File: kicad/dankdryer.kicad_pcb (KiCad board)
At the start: 2 copper layers, 100 x 75 mm, 42 parts, among them J1 Barreljack, J2 upper fan, J3 lower fan, J4 heater, J6 Screw_Terminal_01x05, J7 5kg load cell, J8 motor, J9 Conn_01x04, Q2 SSM3K127TU, Q3 T1210-800G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

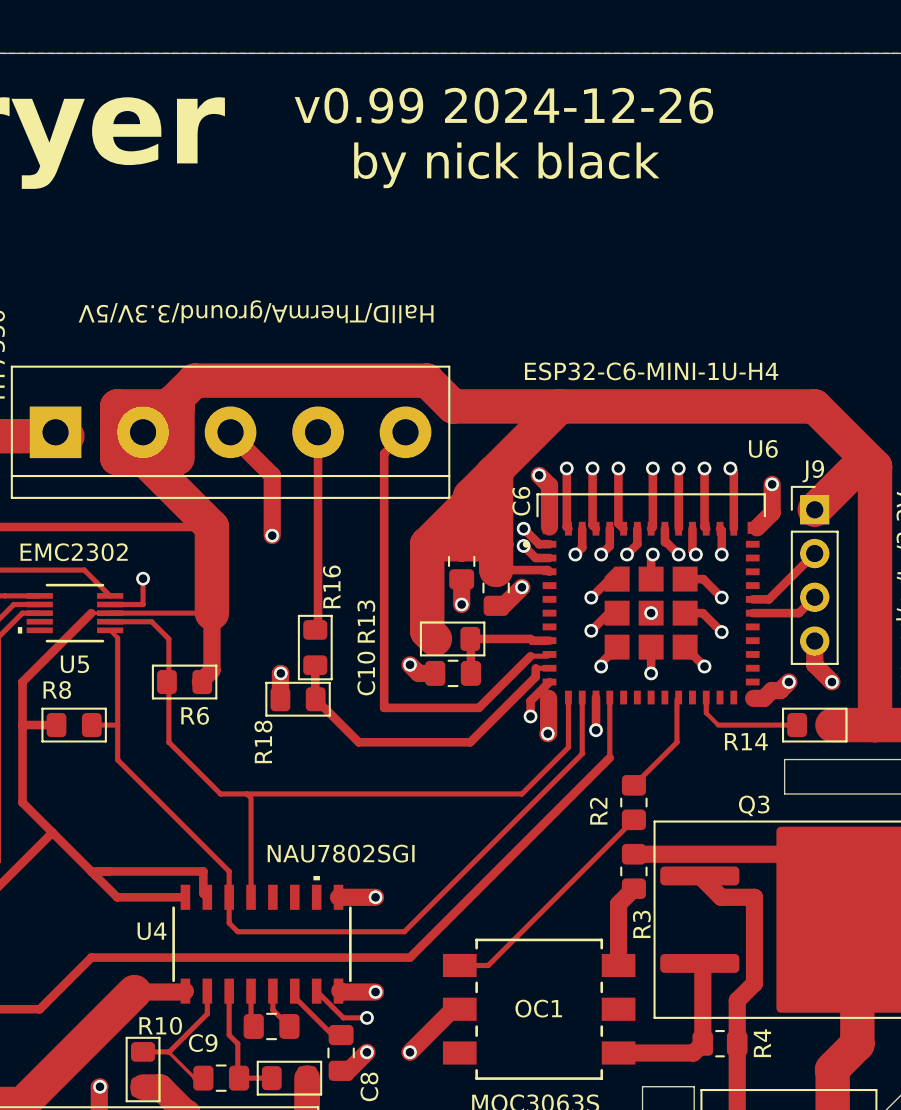
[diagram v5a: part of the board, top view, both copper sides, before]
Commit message: get off the strapping pins. hardware version 1.0
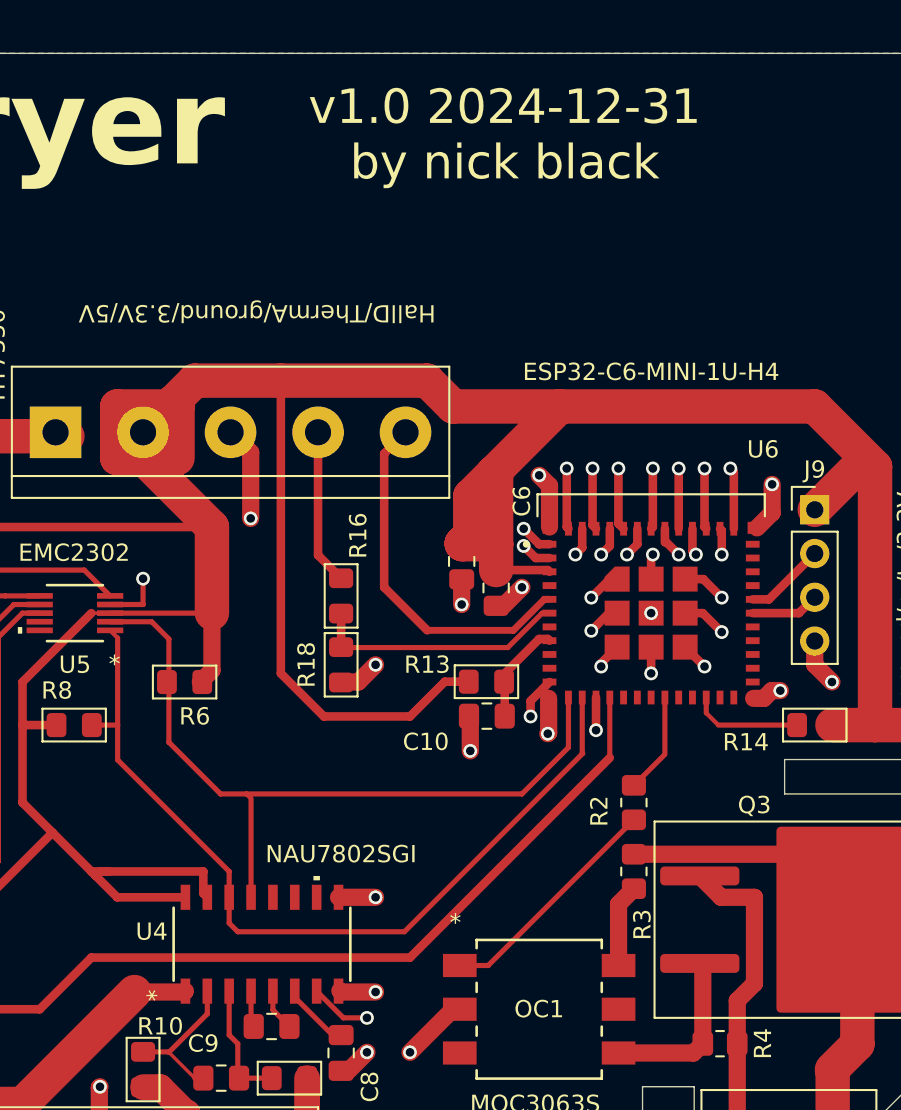
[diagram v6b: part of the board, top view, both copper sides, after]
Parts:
- moved R16 3.35 mm to (105.5, 81.5)
- moved R18 3.20 mm to (105.5, 85.5), turned to 90 degrees
- moved C10 3.16 mm to (114.0, 88.5)
- moved R13 3.16 mm to (113.9, 86.5)
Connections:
- U6 pad 10: /Therm -> unconnected-(U6-IO5-Pad10)
- U6 pad 19: unconnected-(U6-IO14-Pad19) -> /SSRControl
- U6 pad 20: /SSRControl -> unconnected-(U6-IO15-Pad20)
- U6 pad 5: unconnected-(U6-IO2-Pad5) -> /Hall
- U6 pad 6: unconnected-(U6-IO3-Pad6) -> /Therm
- U6 pad 9: /Hall -> unconnected-(U6-IO4-Pad9)
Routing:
- net +3.3V: track 349.1 -> 370.3 mm
- net /Hall: track 27.3 -> 20.9 mm
- net /Therm: track 18.6 -> 14.9 mm
- net /Hot chamber microboard/ThermAnalog: track 11.3 -> 9.03 mm
- net Net-(U6-EN): track 6.60 -> 5.49 mm
- net GND: track 139.5 -> 138.6 mm
- added copper zone on B.Cu, net unconnected-(U2-Therm-Pad9)_2
- removed copper zone on B.Cu, net unconnected-(U2-Therm-Pad9)_3
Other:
- board text added: "v1.0 2024-12-31 by nick black"
- board text removed: "v0.99 2024-12-26 by nick black"

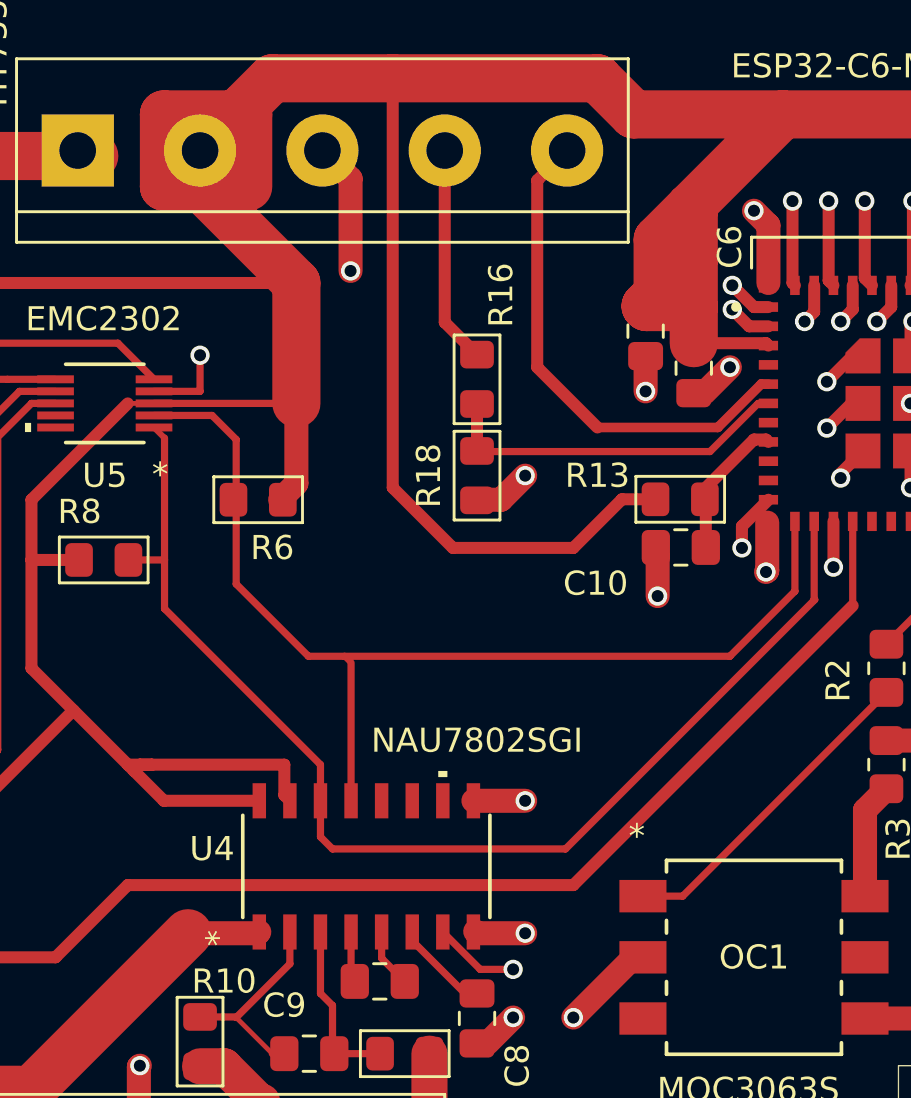
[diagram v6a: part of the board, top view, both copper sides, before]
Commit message: webpage: update copyrights
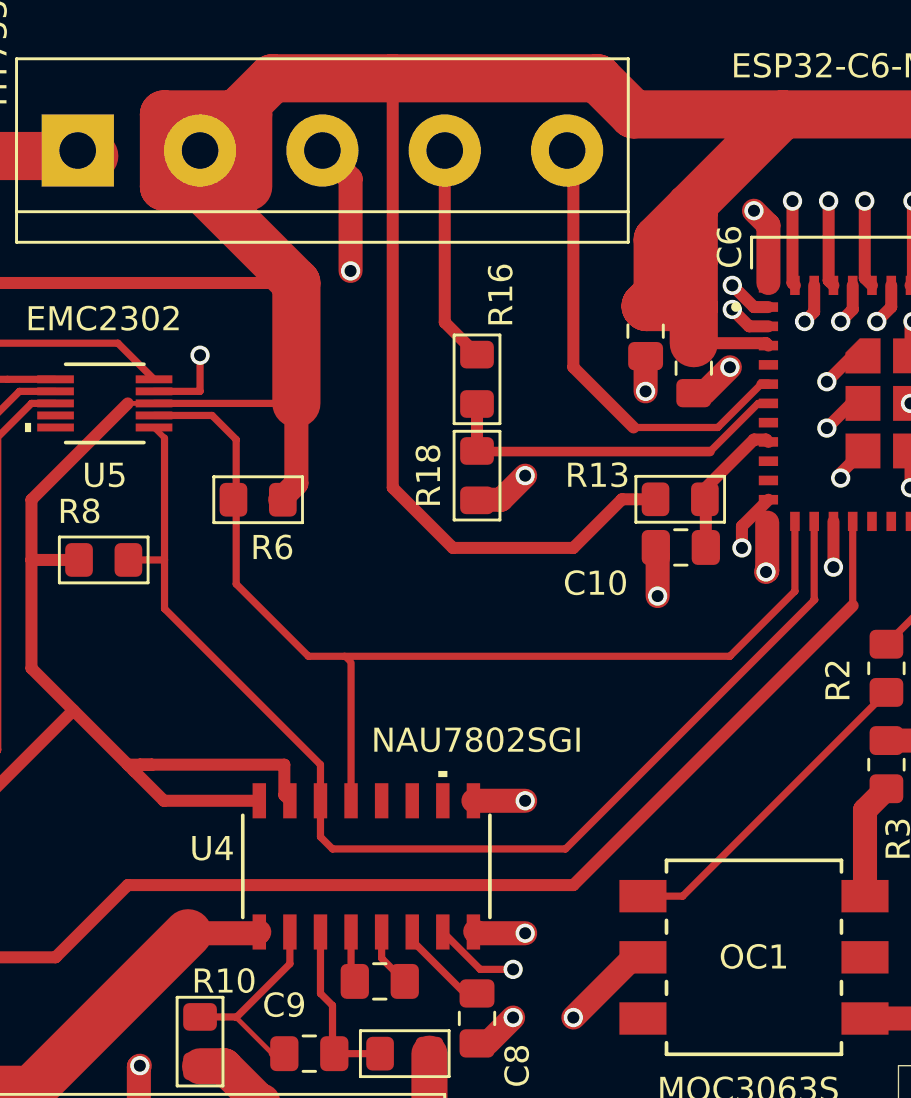
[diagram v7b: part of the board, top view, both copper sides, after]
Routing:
- net /Hall: track 20.9 -> 18.6 mm
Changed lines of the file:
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@@
 			(sketchpadsonfab no)
 			(subtractmaskfromsilk no)
-			(outputformat 1)
+			(outputformat 4)
 			(mirror no)
 			(drillshape 0)
@@
 		)
 		(fp_text user "*"
-			(at -2.97815 -6.1468 90)
-			(layer "F.SilkS")
-			(effects
-				(font
-					(size 1 1)
-					(thickness 0.15)
-				)
-			)
-		)
-		(fp_text user "*"
-			(at -2.97815 -6.1468 90)
-			(layer "F.SilkS")
-			(effects
-				(font
-					(size 1 1)
-					(thickness 0.15)
-				)
-			)
-		)
-		(fp_text user "*"
 			(at -1.6129 -4.9276 90)
 			(layer "F.Fab")
@@
 		)
 		(fp_text user "*"
-			(at -4.8641 -5.0292 0)
-			(layer "F.SilkS")
-			(effects
-				(font
-					(size 1 1)
-					(thickness 0.15)
-				)
-			)
-		)
-		(fp_text user "*"
-			(at -4.8641 -5.0292 0)
-			(layer "F.SilkS")
-			(effects
-				(font
-					(size 1 1)
-					(thickness 0.15)
-				)
-			)
-		)
-		(fp_text user "*"
 			(at -3.1242 -3.8227 0)
 			(layer "F.Fab")
@@
 		)
 		(fp_text user "*"
-			(at -2.2987 -2.4732 180)
-			(unlocked yes)
-			(layer "F.SilkS")
-			(effects
-				(font
-					(size 1 1)
-					(thickness 0.15)
-				)
-			)
-		)
-		(fp_text user "*"
-			(at -2.2987 -2.4732 180)
-			(unlocked yes)
-			(layer "F.SilkS")
-			(effects
-				(font
-					(size 1 1)
-					(thickness 0.15)
-				)
-			)
-		)
-		(fp_text user "*"
 			(at -1.1176 -1.4224 180)
 			(unlocked yes)
@@
 		(start 117.3 81.7)
 		(end 115.5 83.5)
-		(width 0.4)
+		(width 0.3)
 		(layer "F.Cu")
 		(net 62)
 	)
 	(segment
-		(start 108 73.24)
-		(end 108 81)
-		(width 0.5)
+		(start 115.5 83.5)
+		(end 112 83.5)
+		(width 0.3)
 		(layer "F.Cu")
 		(net 62)
 	)
 	(segment
-		(start 108 81)
-		(end 110.5 83.5)
+		(start 109.5 81)
+		(end 109.5 72.26)
 		(width 0.5)
 		(layer "F.Cu")
@@
 	)
 	(segment
-		(start 109.24 72)
-		(end 108 73.24)
+		(start 109.5 81)
+		(end 112 83.5)
 		(width 0.5)
 		(layer "F.Cu")
@@
 	)
 	(segment
-		(start 115.5 83.5)
-		(end 110.5 83.5)
-		(width 0.4)
-		(layer "F.Cu")
-		(net 62)
-	)
-	(segment
 		(start 117.17458 82.5)
 		(end 117.6 82.5)
@@
 		(start 105.525 84.5)
 		(end 115.17458 84.5)
-		(width 0.3)
+		(width 0.4)
 		(layer "F.Cu")
 		(net 63)

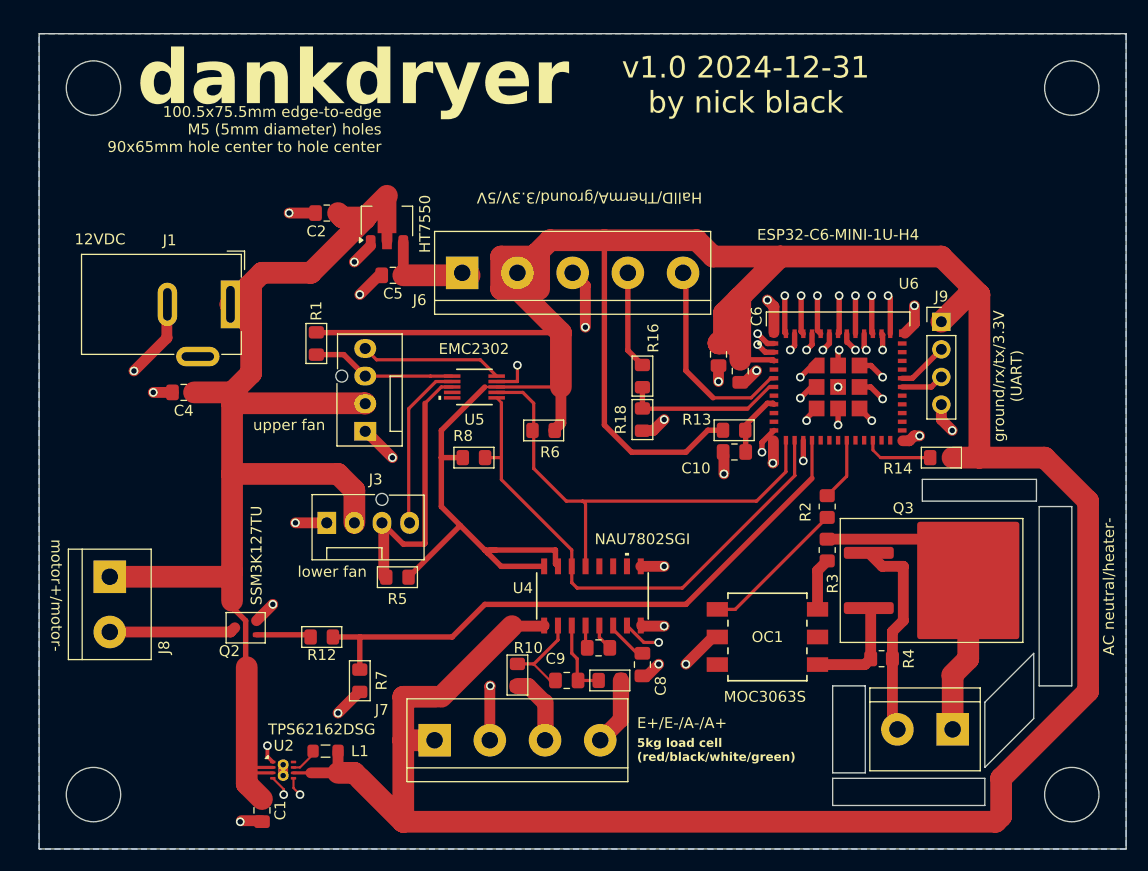
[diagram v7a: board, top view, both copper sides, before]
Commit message: tighten up pcb a bit more
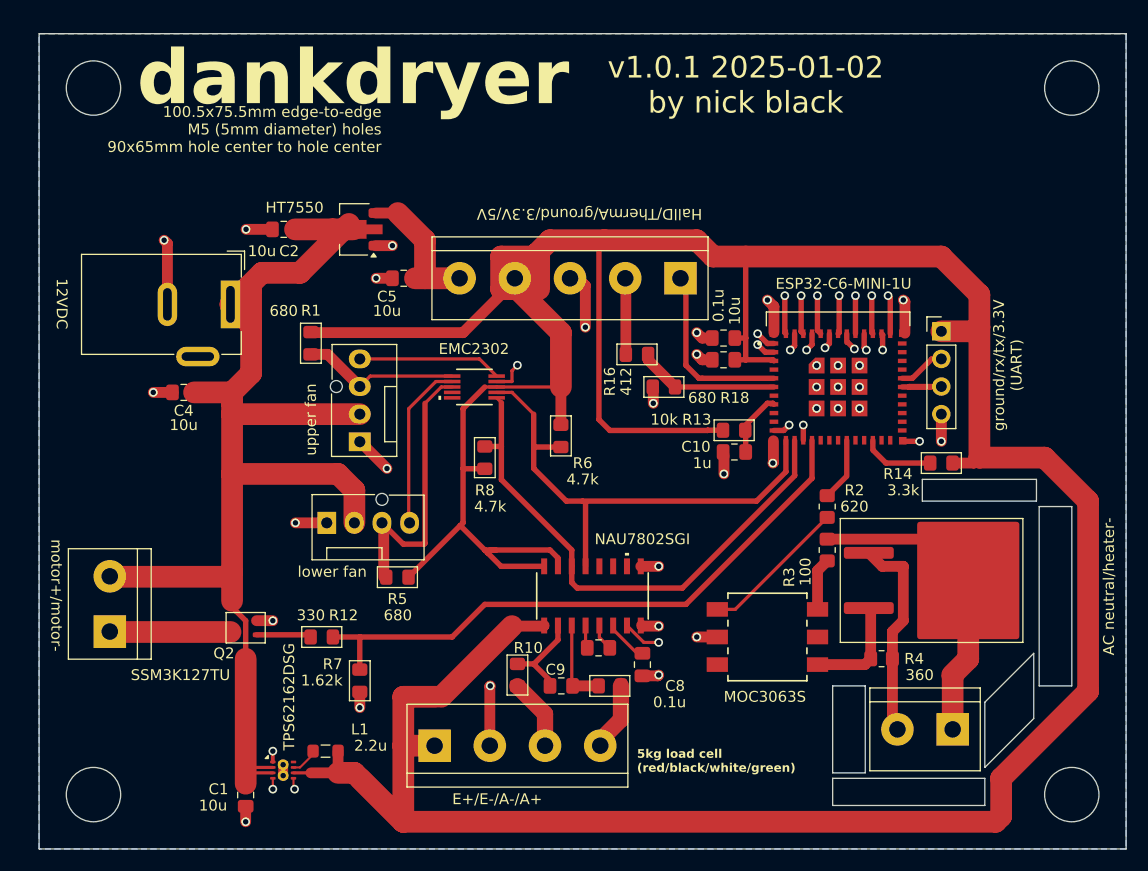
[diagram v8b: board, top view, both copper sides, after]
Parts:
- U6: value ESP32-C6-MINI-1U-H4 -> ESP32-C6-MINI-1U
- moved J6 20.1 mm to (109.0, 72.5), turned to 180 degrees
- moved J8 5.04 mm to (56.5, 105.0), turned to 90 degrees
- moved C2 4.24 mm to (72.5, 68.0)
- moved R18 3.59 mm to (107.5, 82.5), turned to 0 degrees
- moved U3 3.10 mm to (79.0, 68.0), turned to 180 degrees
- moved R16 2.06 mm to (105.0, 79.5), turned to 180 degrees
- moved C1 2.06 mm to (69.0, 120.0)
- moved C6 1.85 mm to (113.0, 80.0), turned to 180 degrees
- moved R6 1.66 mm to (98.0, 87.0), turned to -90 degrees
- moved C3 1.57 mm to (113.0, 78.0), turned to 180 degrees
- moved J2 1.08 mm to (79.5, 87.5)
- moved C5 1.02 mm to (83.5, 72.5)
- moved R8 1.00 mm to (91.0, 89.0), turned to 90 degrees
- moved J9 0.88 mm to (133.0, 77.4)
- moved C9 0.71 mm to (98.0, 110.0)
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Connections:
- J6 pad 1: +5VA -> /Hall
- J6 pad 2: +3.3V -> /Hot chamber microboard/ThermAnalog
- J6 pad 4: /Hot chamber microboard/ThermAnalog -> +3.3V
- J6 pad 5: /Hall -> +5VA
- J8 pad 1: +12V -> /Motor-
- J8 pad 2: /Motor- -> +12V
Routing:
- net GND: track 138.6 -> 110.7 mm
- net +3.3V: track 370.3 -> 352.6 mm
- net +12V: track 123.5 -> 114.2 mm
- net +5VA: track 9.16 -> 13.2 mm
- net /Hot chamber microboard/ThermAnalog: track 9.03 -> 6.94 mm
- net /SCL: track 44.4 -> 46.3 mm
- net /Hall: track 18.6 -> 16.8 mm
- net /Therm: track 14.9 -> 13.1 mm
- net /RXD0: track 3.98 -> 5.70 mm
- net Net-(J2-Pin_3): track 13.3 -> 14.6 mm
- net /Motor-: track 11.7 -> 11.1 mm
- net Net-(U4-VIN1N): track 8.61 -> 8.11 mm
- net /A+: track 6.29 -> 5.79 mm
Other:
- board text added: "v1.0.1 2025-01-02 by nick black"
- board text removed: "v1.0 2024-12-31 by nick black"
